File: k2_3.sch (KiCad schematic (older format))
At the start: 29 parts, among them IC3 TL074, J10 PJ301_THONKICONN6, J11 PJ301_THONKICONN6, J12 PJ301_THONKICONN6, J15 Conn_01x05_Female, J18 Conn_01x05_Male, J9 PJ301_THONKICONN6, Q1 MMBFJ309, Q2 MMBT3904, Q3 MMBT3904

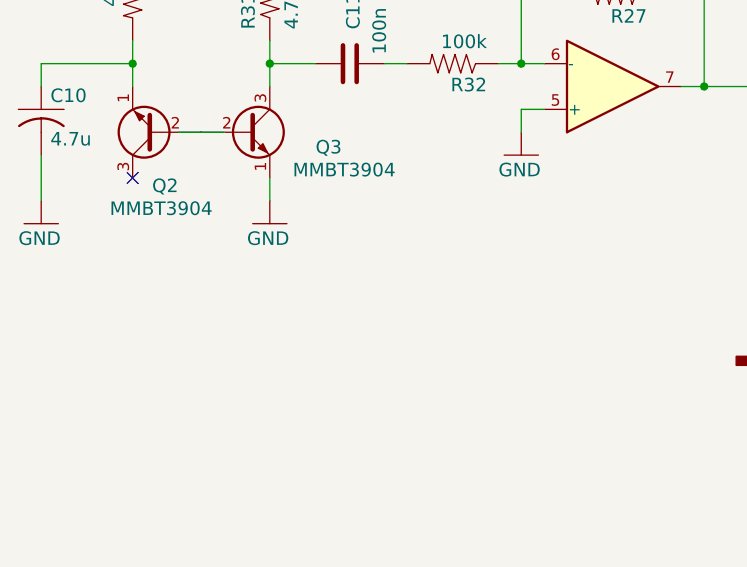
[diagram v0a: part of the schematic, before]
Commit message: dec2021
status after testing v101
found errors in this board
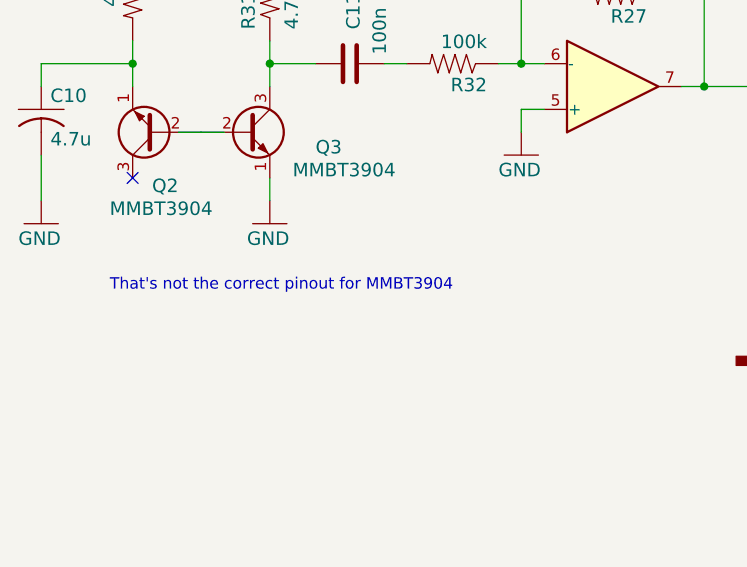
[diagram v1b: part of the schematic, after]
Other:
- note added: "That's not the correct pinout for MMBT3904"
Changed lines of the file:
@@
 Text Notes 7350 2900 0    50   ~ 0
 123 = SDG
+Text Notes 2100 2800 0    50   ~ 0
+That's not the correct pinout for MMBT3904
 $EndSCHEMATC

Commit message: upd to board 1.2
should fix transistor footprint and shift diodes
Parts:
- Q2, Q3: symbol device:Q_NPN_EBC -> device:Q_NPN_BEC
- R27: value 1.5M -> 1M
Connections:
- net at C10.1, R30.2: now also Q2.2 (E); no longer Q2.1 (E)
- net at Q3.2 (E): no longer Q2.2 (B)
- net at Q3.1 (B): now also Q2.1 (B)
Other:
- note added: "R27 sets noise level\noriginal was 1.5M but the resulting 18vpp was problematic\nnow 1M gives about 12Vpp which is great"
- note added: "That's not the correct pinout for MMBT3904\nhad to install them upside down to flip B/E"
- note added: "special C0G 10nF for better hold time"
- note added: "this circuit had a decoupler \nbetween its r25 and vcc (here R26)\nspecced at 4u7 tant\nremoved because i dont know what it was for"
- note removed: "That's not the correct pinout for MMBT3904"
- note removed: "this circuit had a decoupler \nbetween r25 and vcc \nspecced at 4u7 tant\nremoved because i dont know what it was for"
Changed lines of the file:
@@
 Title "Crimps"
 Date "2021-11-12"
-Rev "101"
+Rev "1.2.1"
 Comp "Karltron.com"
 Comment1 ""
@@
 AR Path="/61897122/E6329875" Ref="R27"  Part="1"
 F 0 "R27" H 4150 1559 59  0000 L BNN
-F 1 "1.5M" H 4150 1370 59  0000 L BNN
+F 1 "1M" H 4150 1370 59  0000 L BNN
 F 2 "Resistor_SMD:R_0805_2012Metric_Pad1.20x1.40mm_HandSolder" H 4300 1500 50  0001 C CNN
 F 3 "" H 4300 1500 50  0001 C CNN
@@
 $EndComp
 $Comp
-L device:Q_NPN_EBC Q2
+L device:Q_NPN_BEC Q2
 U 1 1 5C6CF9B0
 P 2300 2100
@@
 $EndComp
 $Comp
-L device:Q_NPN_EBC Q3
+L device:Q_NPN_BEC Q3
 U 1 1 FFA79A6C
 P 2700 2100
@@
 rewrite by karl.stamm@gmail.com\nfor DIY / SMD0805 hand craft in two panels\nkarltron.com\ngithub.com/kstammits
 Text Notes 6300 4500 0    50   ~ 0
-this circuit had a decoupler \nbetween r25 and vcc \nspecced at 4u7 tant\nremoved because i dont know what it was for
+this circuit had a decoupler \nbetween its r25 and vcc   (here R26)\nspecced at 4u7 tant\nremoved because i dont know what it was for
 Wire Wire Line
 	4100 5100 4150 5100
@@
 123 = SDG
 Text Notes 2100 2800 0    50   ~ 0
-That's not the correct pinout for MMBT3904
+That's not the correct pinout for MMBT3904\nhad to install them upside down to flip B/E
+Text Notes 3950 1300 0    50   ~ 0
+R27 sets noise level\noriginal was 1.5M but the resulting 18vpp was problematic\nnow 1M gives about 12Vpp which is great
+Text Notes 7800 3450 0    50   ~ 0
+special C0G 10nF for better hold time
 $EndSCHEMATC

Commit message: printing pretty schem
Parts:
- IC3: value TL074 -> OPA4171
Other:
- note added: "other jfets seem to work\ntesting ..."
- note removed: "That's not the correct pinout for MMBT3904\nhad to install them upside down to flip B/E"
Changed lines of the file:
@@
 AR Path="/C31D8B89" Ref="IC3"  Part="1"
 AR Path="/61897122/C31D8B89" Ref="IC3"  Part="1"
-F 0 "IC3" H 6600 3025 59  0001 L BNN
-F 1 "TL074" H 6600 2700 59  0001 L BNN
+F 0 "IC3" H 6600 3025 59  0000 L BNN
+F 1 "OPA4171" H 6600 2700 59  0000 L BNN
 F 2 "Package_SO:SOIC-14_3.9x8.7mm_P1.27mm" H 6500 2900 50  0001 C CNN
 F 3 "" H 6500 2900 50  0001 C CNN
@@
 AR Path="/6191608E" Ref="IC?"  Part="1"
 AR Path="/61897122/6191608E" Ref="IC3"  Part="2"
-F 0 "IC3" H 4400 2025 59  0001 L BNN
-F 1 "TL074" H 4400 1700 59  0001 L BNN
+F 0 "IC3" H 4400 2025 59  0000 L BNN
+F 1 "OPA4171" H 4400 1700 59  0000 L BNN
 F 2 "Package_SO:SOIC-14_3.9x8.7mm_P1.27mm" H 4300 1900 50  0001 C CNN
 F 3 "" H 4300 1900 50  0001 C CNN
@@
 AR Path="/61919844" Ref="IC?"  Part="1"
 AR Path="/61897122/61919844" Ref="IC3"  Part="3"
-F 0 "IC3" H 6600 5125 59  0001 L BNN
-F 1 "TL074" H 6600 4800 59  0001 L BNN
+F 0 "IC3" H 6600 5125 59  0000 L BNN
+F 1 "OPA4171" H 6600 4800 59  0000 L BNN
 F 2 "Package_SO:SOIC-14_3.9x8.7mm_P1.27mm" H 6500 5000 50  0001 C CNN
 F 3 "" H 6500 5000 50  0001 C CNN
@@
 AR Path="/6191CC51" Ref="IC?"  Part="1"
 AR Path="/61897122/6191CC51" Ref="IC3"  Part="4"
-F 0 "IC3" H 8300 2925 59  0001 L BNN
-F 1 "TL074" H 8300 2600 59  0001 L BNN
+F 0 "IC3" H 8300 2925 59  0000 L BNN
+F 1 "OPA4171" H 8300 2600 59  0000 L BNN
 F 2 "Package_SO:SOIC-14_3.9x8.7mm_P1.27mm" H 8200 2800 50  0001 C CNN
 F 3 "" H 8200 2800 50  0001 C CNN
@@
 Text Notes 7350 2900 0    50   ~ 0
 123 = SDG
-Text Notes 2100 2800 0    50   ~ 0
-That's not the correct pinout for MMBT3904\nhad to install them upside down to flip B/E
 Text Notes 3950 1300 0    50   ~ 0
 R27 sets noise level\noriginal was 1.5M but the resulting 18vpp was problematic\nnow 1M gives about 12Vpp which is great
 Text Notes 7800 3450 0    50   ~ 0
 special C0G 10nF for better hold time
+Text Notes 7250 2250 0    50   ~ 0
+other jfets seem to work\ntesting ...
 $EndSCHEMATC

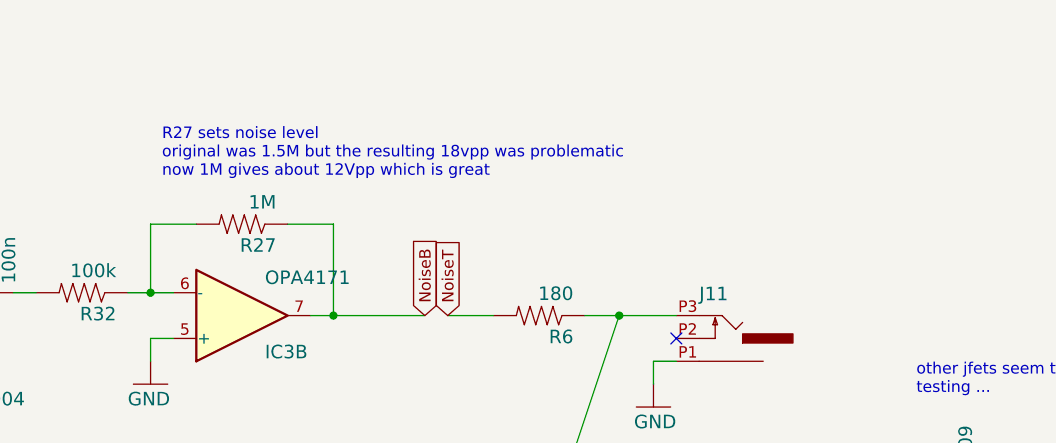
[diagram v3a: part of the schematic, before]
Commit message: update for noise level
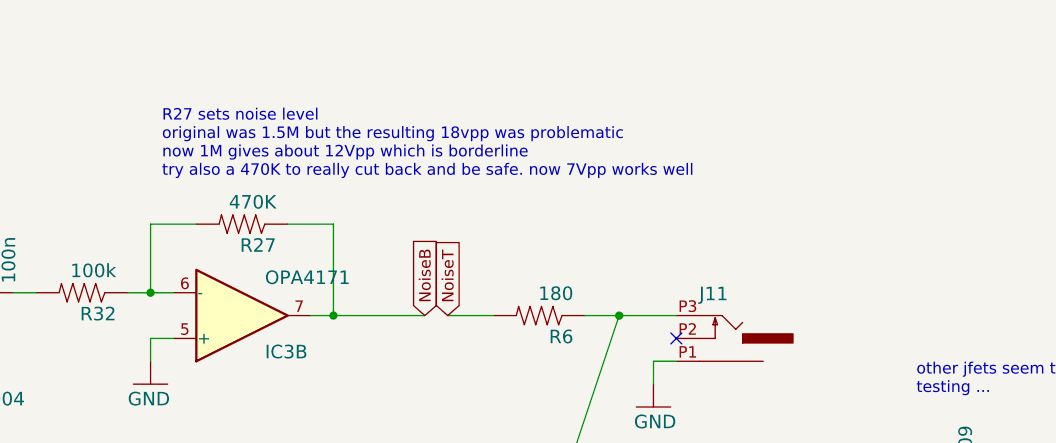
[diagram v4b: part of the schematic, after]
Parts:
- R27: value 1M -> 470K
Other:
- note added: "R27 sets noise level\noriginal was 1.5M but the resulting 18vpp was problematic\nnow 1M gives about 12Vpp which is borderline\ntry also a 470K to really cut back and be safe. now 7Vpp works well"
- note removed: "R27 sets noise level\noriginal was 1.5M but the resulting 18vpp was problematic\nnow 1M gives about 12Vpp which is great"
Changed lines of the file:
@@
 AR Path="/61897122/E6329875" Ref="R27"  Part="1"
 F 0 "R27" H 4150 1559 59  0000 L BNN
-F 1 "1M" H 4150 1370 59  0000 L BNN
+F 1 "470K" H 4150 1370 59  0000 L BNN
 F 2 "Resistor_SMD:R_0805_2012Metric_Pad1.20x1.40mm_HandSolder" H 4300 1500 50  0001 C CNN
 F 3 "" H 4300 1500 50  0001 C CNN
@@
 123 = SDG
 Text Notes 3950 1300 0    50   ~ 0
-R27 sets noise level\noriginal was 1.5M but the resulting 18vpp was problematic\nnow 1M gives about 12Vpp which is great
+R27 sets noise level\noriginal was 1.5M but the resulting 18vpp was problematic\nnow 1M gives about 12Vpp which is borderline\ntry also a 470K to really cut back and be safe. now 7Vpp works well
 Text Notes 7800 3450 0    50   ~ 0
 special C0G 10nF for better hold time
